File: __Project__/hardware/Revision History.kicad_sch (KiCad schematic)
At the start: 0 parts

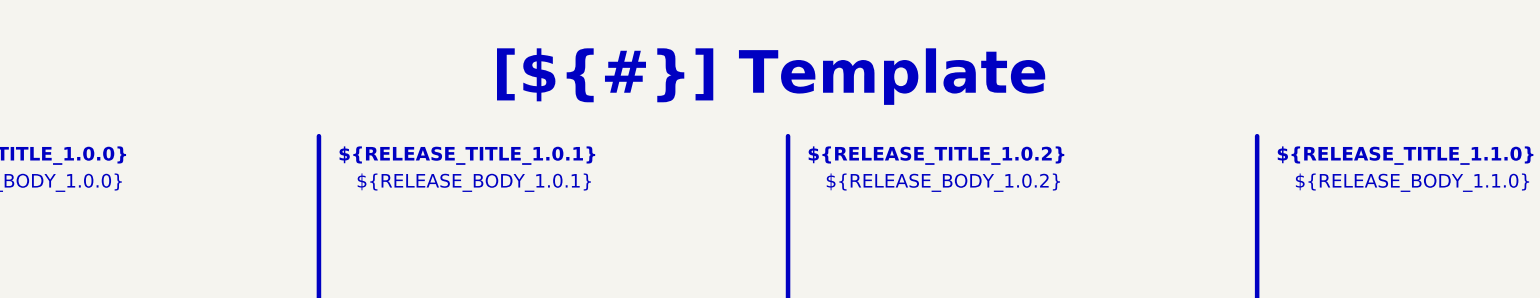
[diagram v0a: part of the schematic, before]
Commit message: Fix JST footprints
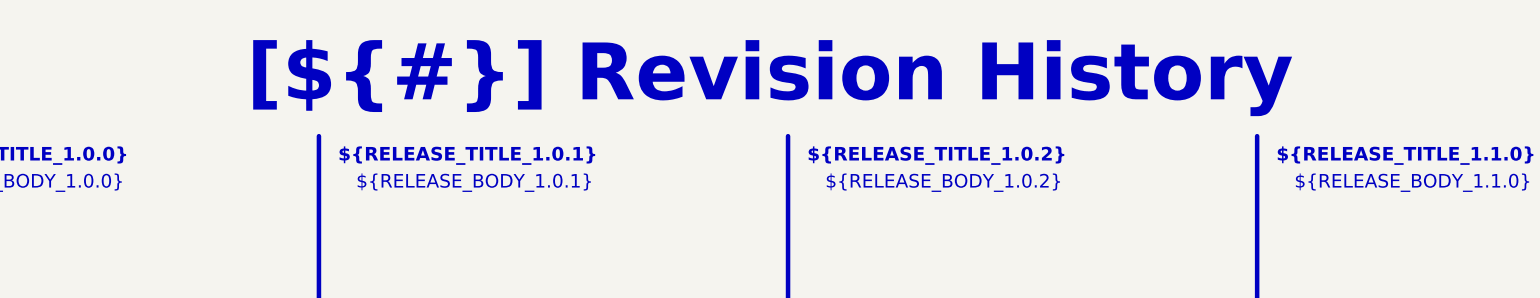
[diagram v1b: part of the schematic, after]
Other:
- title: Template -> Revision History
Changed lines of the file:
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@@
 	(paper "A4")
 	(title_block
-		(title "Template")
+		(title "Revision History")
 		(date "2025-06-05")
 		(rev "${REVISION}")
@@
 	(text_box "[${#}] ${TITLE}"
 		(exclude_from_sim no)
-		(at 80.01 16.51 0)
-		(size 137.16 12.7)
-		(margins 4.4999 4.4999 4.4999 4.4999)
+		(at 12.7 12.7 0)
+		(size 271.78 20.32)
+		(margins 5.9999 5.9999 5.9999 5.9999)
 		(stroke
 			(width -0.0001)
@@
 			(font
 				(face "Times New Roman")
-				(size 6 6)
+				(size 8 8)
 				(thickness 1.2)
 				(bold yes)
